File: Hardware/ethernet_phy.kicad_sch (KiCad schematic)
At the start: 29 parts, among them J5 WE-RJ45_7499010211A, U6 DP83822IRHBR

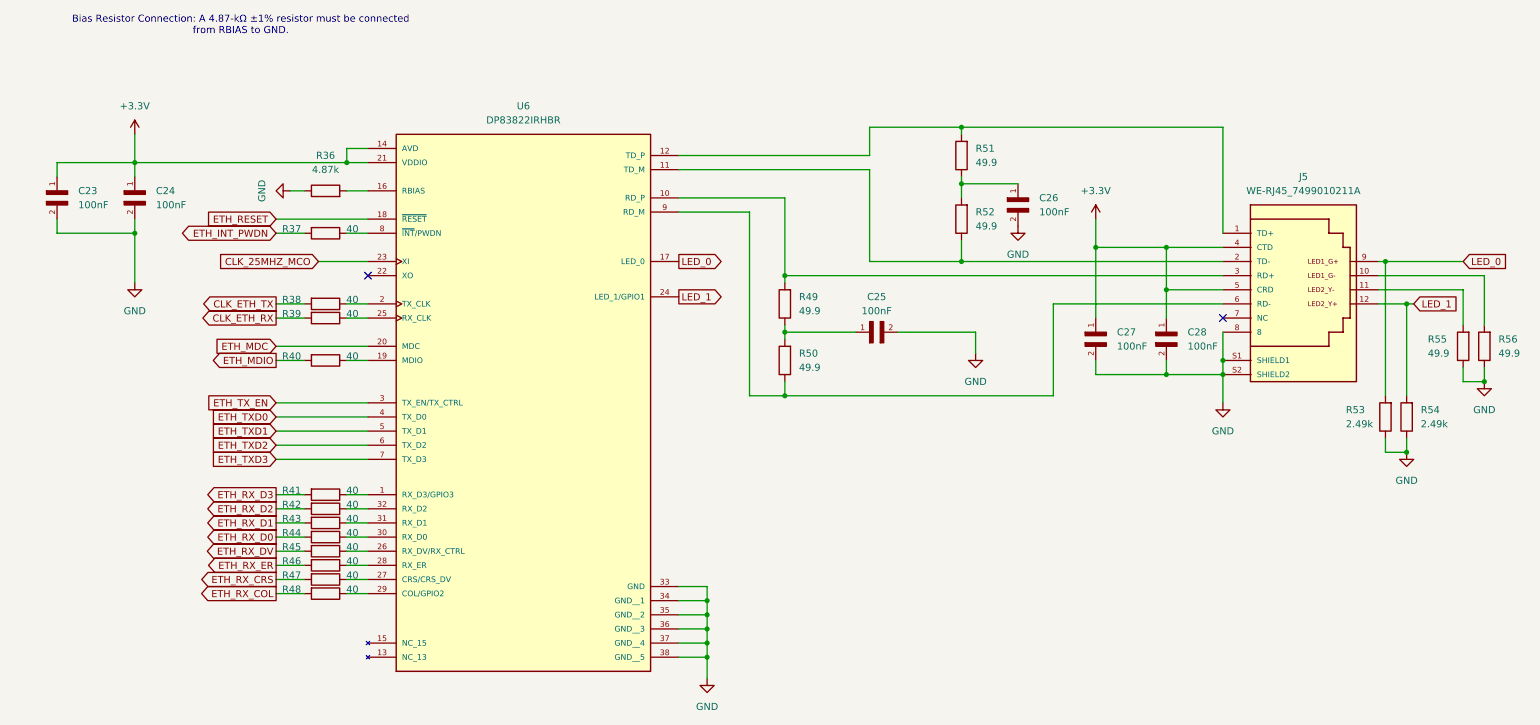
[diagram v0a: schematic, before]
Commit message: added stackup doc and reduced board to 10 layers
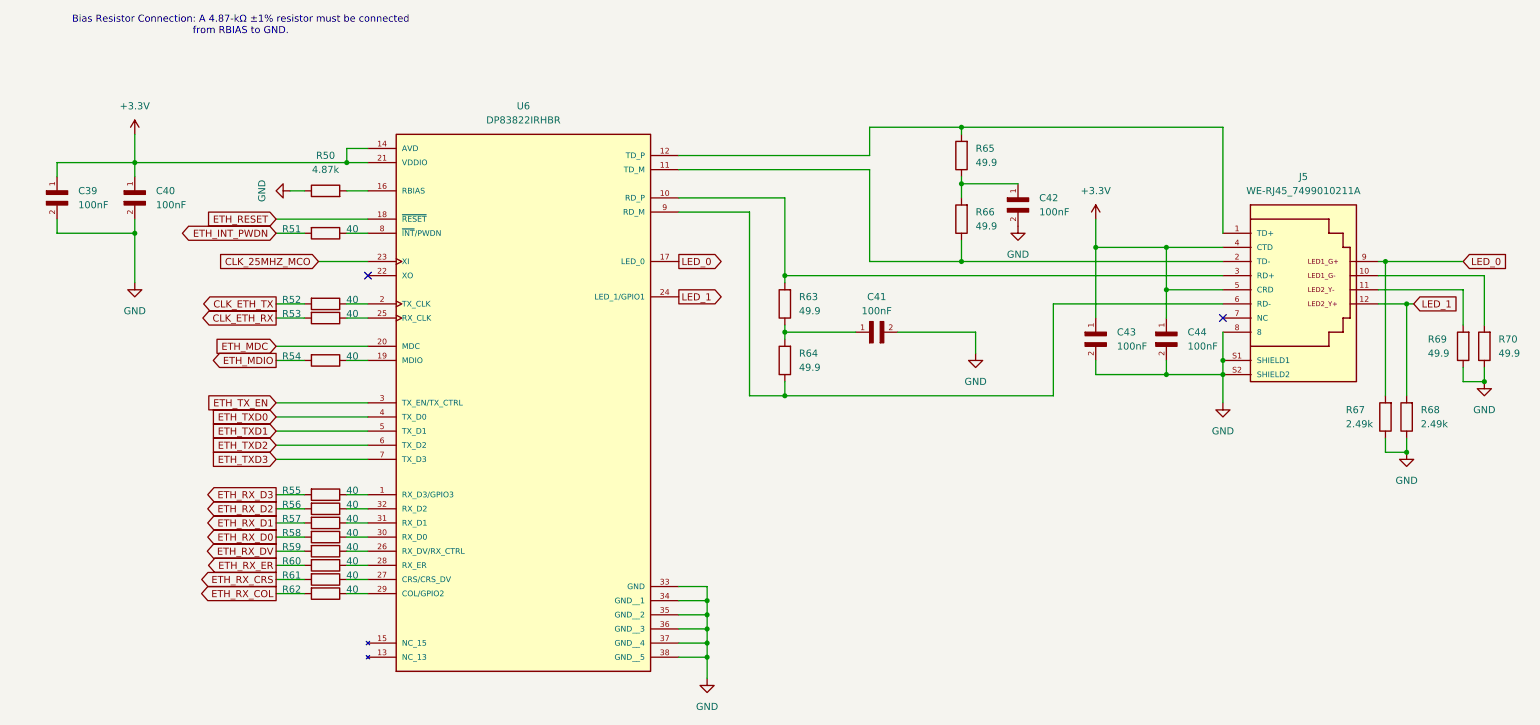
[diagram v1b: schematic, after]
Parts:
- renumbered C23 to C39, C24 to C40, C25 to C41, C26 to C42, C27 to C43, C28 to C44, R36 to R50, R37 to R51, R38 to R52, R39 to R53, R40 to R54, R41 to R55, R42 to R56, R43 to R57, R44 to R58, R45 to R59, R46 to R60, R47 to R61, R48 to R62, R49 to R63, R50 to R64, R51 to R65, R52 to R66, R53 to R67, R54 to R68, R55 to R69, R56 to R70

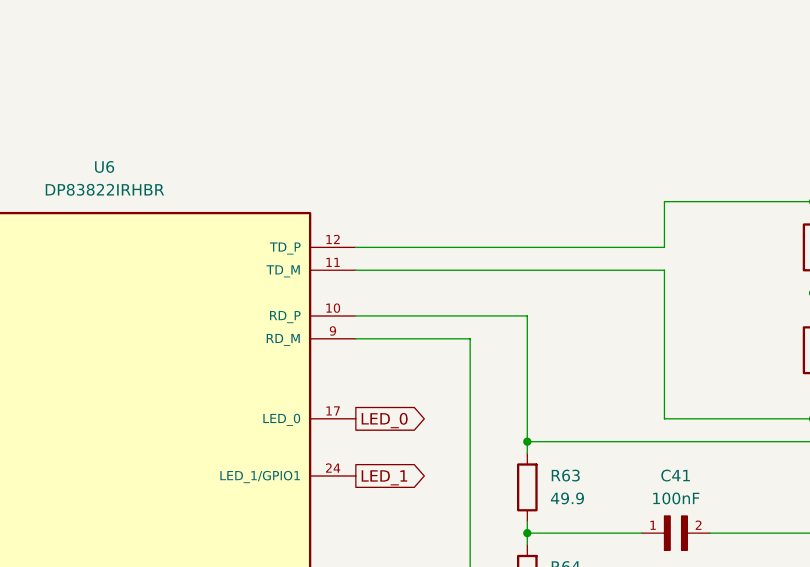
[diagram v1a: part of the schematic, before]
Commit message: fixed USB data lines and directory hierarchy
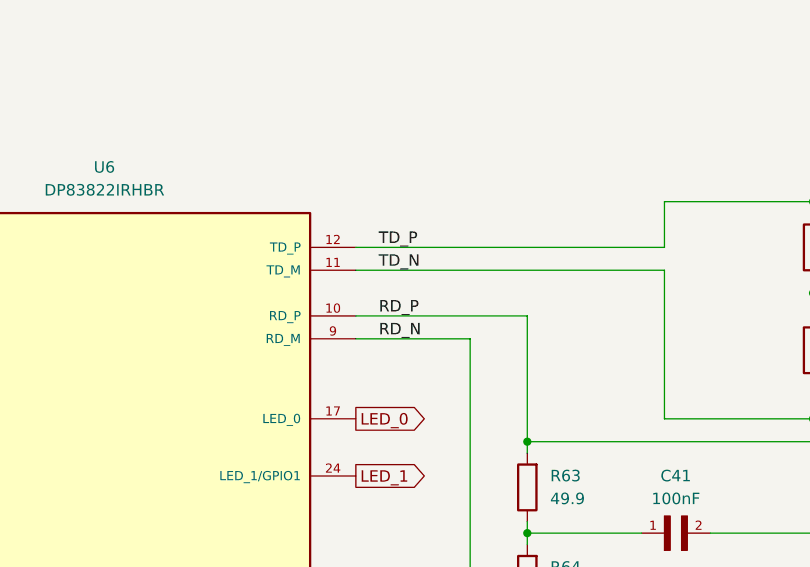
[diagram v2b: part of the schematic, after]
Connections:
- net RD_P: now reaches J5.3 (RD+), R63.2, U6.10 (RD_P)
- net TD_N: now reaches J5.2 (TD-), R66.1, U6.11 (TD_M)
- net TD_P: now reaches J5.1 (TD+), R65.2, U6.12 (TD_P)
- net RD_N: now reaches J5.6 (RD-), R64.1, U6.9 (RD_M)
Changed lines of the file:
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@@
+		)
+	)
+	(label "RD_N"
+		(at 132.08 53.34 0)
+		(effects
+			(font
+				(size 1.27 1.27)
+			)
+			(justify left bottom)
+		)
+	)
+	(label "RD_P"
+		(at 132.08 50.8 0)
+		(effects
+			(font
+				(size 1.27 1.27)
+			)
+			(justify left bottom)
+		)
+	)
+	(label "TD_N"
+		(at 132.08 45.72 0)
+		(effects
+			(font
+				(size 1.27 1.27)
+			)
+			(justify left bottom)
+		)
+	)
+	(label "TD_P"
+		(at 132.08 43.18 0)
+		(effects
+			(font
+				(size 1.27 1.27)
+			)
+			(justify left bottom)
 		)
 	)
